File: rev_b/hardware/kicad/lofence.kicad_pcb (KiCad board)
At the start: 2 copper layers, 78 x 130 mm, 65 parts, among them J1 Fence+, J2 Fence-, J3 ISP, J4 DEBUG RN, J5 DEBUG LED, J6 DEBUG MCU, J7 868, J8 PWR, SW1 RESET, U1 Opamp_Dual_Generic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

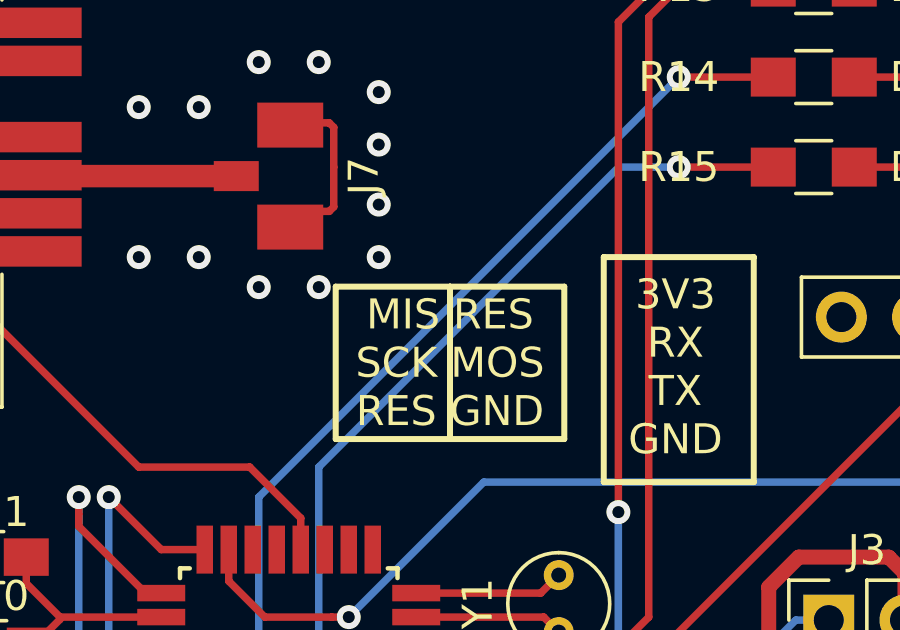
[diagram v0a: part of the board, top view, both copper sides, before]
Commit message: Fixed silkscreen for ISP connector
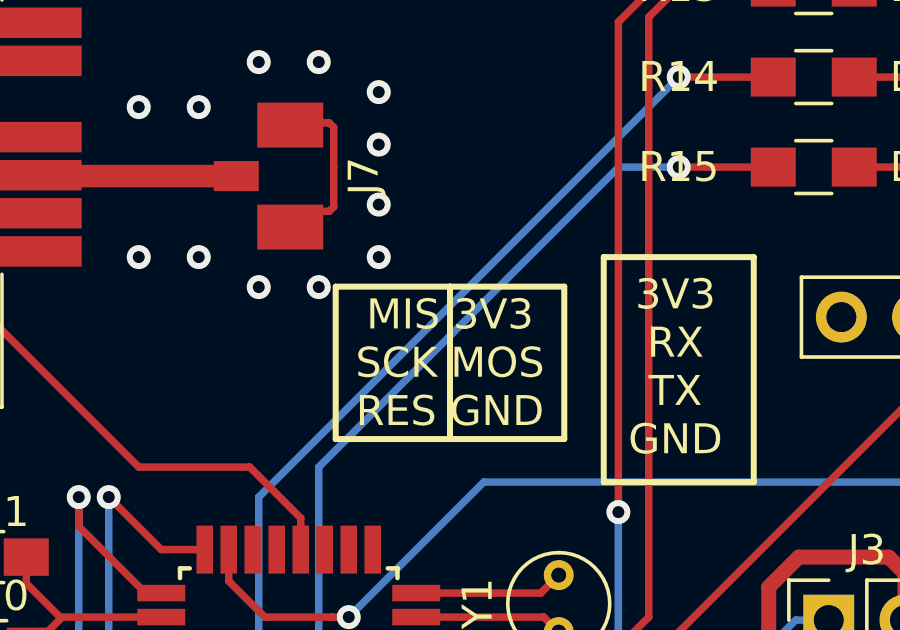
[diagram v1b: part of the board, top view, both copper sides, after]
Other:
- board text added: "MIS 3V3 SCK MOS RES GND"
- board text removed: "MIS RES SCK MOS RES GND"
